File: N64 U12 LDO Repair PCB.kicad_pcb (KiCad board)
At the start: 2 copper layers, 8.5 x 7 mm, 5 parts, among them J1 Conn_01x05_Pin, U1 TLV78525PDBVR

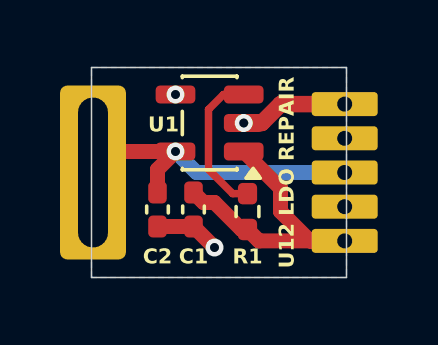
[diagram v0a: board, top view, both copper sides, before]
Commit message: Revision 1: Fix pin pitch
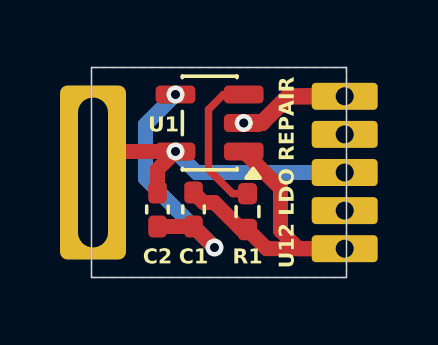
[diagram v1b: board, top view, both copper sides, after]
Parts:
- C2: value 4.7 uF -> 1 uF
- J1: footprint Custom:CustomAdapter_TO-252-5 -> Custom:CustomAdapter_SharpPQ7VZ5
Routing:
- net GND: track 5.82 -> 12.4 mm
- net +3V3: track 10.9 -> 11.4 mm
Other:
- board text added: "Rev. 1"
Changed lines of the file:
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@@
 			)
 		)
-		(property "Value" "4.7 uF"
+		(property "Value" "1 uF"
 			(at 0 1.16 90)
 			(layer "F.Fab")
@@
 		)
 	)
-	(footprint "Custom:CustomAdapter_TO-252-5"
+	(footprint "Custom:CustomAdapter_SharpPQ7VZ5"
 		(layer "F.Cu")
 		(at 50 50 180)
@@
 		(tags "DPAK TO-252 DPAK-5 TO-252-5")
 		(property "Reference" "J1"
-			(at 0 -4.5 0)
+			(at 0 -4.5 180)
 			(layer "F.SilkS")
 			(hide yes)
@@
 		)
 		(property "Value" "Conn_01x05_Pin"
-			(at 0 4.5 0)
+			(at 0 4.5 180)
 			(layer "F.Fab")
 			(effects
@@
 		)
 		(property "Datasheet" ""
-			(at 0 0 0)
+			(at 0 0 180)
 			(layer "F.Fab")
 			(hide yes)
@@
 		)
 		(property "Description" "Generic connector, single row, 01x05, script generated"
-			(at 0 0 0)
+			(at 0 0 180)
 			(layer "F.Fab")
 			(hide yes)
@@
 		)
 		(property "KiLib_Generator" "package/TO_SOT/SMD"
-			(at 0 0 0)
+			(at 0 0 180)
 			(layer "F.SilkS")
 			(hide yes)
@@
 		(sheetname "/")
 		(sheetfile "N64 U12 LDO Repair PCB.kicad_sch")
-		(attr smd exclude_from_bom allow_missing_courtyard dnp)
+		(attr smd allow_missing_courtyard dnp)
 		(duplicate_pad_numbers_are_jumpers no)
 		(fp_line
@@
 		)
 		(fp_text user "${REFERENCE}"
-			(at 0 0 0)
+			(at 0 0 180)
 			(layer "F.Fab")
 			(effects
@@
 		)
 		(pad "1" thru_hole roundrect
-			(at -5.04 -2.28 180)
-			(size 2.2 0.8)
-			(drill 0.5)
+			(at -5.04 -2.54 180)
+			(size 2.2 0.9)
+			(drill 0.6)
 			(property pad_prop_castellated)
 			(layers "*.Cu" "*.Mask")
@@
 		)
 		(pad "2" thru_hole roundrect
-			(at -5.04 -1.14 180)
-			(size 2.2 0.8)
-			(drill 0.5)
+			(at -5.04 -1.27 180)
+			(size 2.2 0.9)
+			(drill 0.6)
 			(property pad_prop_castellated)
 			(layers "*.Cu" "*.Mask")
@@
 		(pad "3" thru_hole roundrect
 			(at -5.04 0 180)
-			(size 2.2 0.8)
-			(drill 0.5)
+			(size 2.2 0.9)
+			(drill 0.6)
 			(property pad_prop_castellated)
 			(layers "*.Cu" "*.Mask")
@@
 		)
 		(pad "4" thru_hole roundrect
-			(at -5.04 1.14 180)
-			(size 2.2 0.8)
-			(drill 0.5)
+			(at -5.04 1.27 180)
+			(size 2.2 0.9)
+			(drill 0.6)
 			(property pad_prop_castellated)
 			(layers "*.Cu" "*.Mask")
@@
 		)
 		(pad "5" thru_hole roundrect
-			(at -5.04 2.28 180)
-			(size 2.2 0.8)
-			(drill 0.5)
+			(at -5.04 2.54 180)
+			(size 2.2 0.9)
+			(drill 0.6)
 			(property pad_prop_castellated)
 			(layers "*.Cu" "*.Mask")
@@
 		)
 	)
-	(segment
-		(start 51.735 51.835)
-		(end 51.8 51.9)
+	(gr_text "Rev. 1"
+		(at 51.1 53.2 -0)
+		(layer "B.SilkS")
+		(effects
+			(font
+				(size 0.5 0.5)
+				(thickness 0.1)
+				(bold yes)
+			)
+			(justify bottom mirror)
+		)
+	)
+	(segment
+		(start 48.835 50.7)
+		(end 48.8 50.665)
+		(width 0.5)
+		(layer "F.Cu")
+		(net "+2V5")
+	)
+	(segment
+		(start 47.35 49.3)
+		(end 46.65 50)
 		(width 0.2)
 		(layer "F.Cu")
-		(net "+3V3")
-	)
-	(segment
-		(start 52.9 51.3)
-		(end 52.9 50.525)
-		(width 0.5)
-		(layer "F.Cu")
-		(net "+3V3")
-	)
-	(segment
-		(start 55.04 52.28)
-		(end 52.18 52.28)
-		(width 0.5)
-		(layer "F.Cu")
-		(net "+3V3")
-	)
-	(segment
-		(start 51.6 51.9)
-		(end 50.7 51)
-		(width 0.5)
-		(layer "F.Cu")
-		(net "+3V3")
-	)
-	(segment
-		(start 55.04 52.28)
-		(end 53.88 52.28)
-		(width 0.5)
-		(layer "F.Cu")
-		(net "+3V3")
-	)
-	(segment
-		(start 53.88 52.28)
-		(end 52.9 51.3)
-		(width 0.5)
-		(layer "F.Cu")
-		(net "+3V3")
-	)
-	(segment
-		(start 50.7 51)
-		(end 50.335 51)
-		(width 0.5)
-		(layer "F.Cu")
-		(net "+3V3")
-	)
-	(segment
-		(start 52.18 52.28)
-		(end 51.8 51.9)
-		(width 0.5)
-		(layer "F.Cu")
-		(net "+3V3")
-	)
-	(segment
-		(start 51.8 51.9)
-		(end 51.6 51.9)
-		(width 0.5)
-		(layer "F.Cu")
-		(net "+3V3")
-	)
-	(segment
-		(start 50.335 51)
-		(end 50 50.665)
-		(width 0.5)
-		(layer "F.Cu")
-		(net "+3V3")
-	)
-	(segment
-		(start 52.9 50.525)
-		(end 51.675 49.3)
-		(width 0.5)
-		(layer "F.Cu")
-		(net "+3V3")
-	)
-	(segment
-		(start 55.04 47.72)
-		(end 52.90554 47.72)
+		(net "+2V5")
+	)
+	(segment
+		(start 49.4 49.3)
+		(end 47.35 49.3)
+		(width 0.5)
+		(layer "F.Cu")
+		(net "+2V5")
+	)
+	(segment
+		(start 48.8 49.9)
+		(end 49.4 49.3)
+		(width 0.5)
+		(layer "F.Cu")
+		(net "+2V5")
+	)
+	(segment
+		(start 48.8 50.665)
+		(end 48.8 49.9)
+		(width 0.5)
+		(layer "F.Cu")
+		(net "+2V5")
+	)
+	(via
+		(at 49.4 49.3)
+		(size 0.6)
+		(drill 0.3)
+		(layers "F.Cu" "B.Cu")
+		(net "+2V5")
+	)
+	(segment
+		(start 50.1 50)
+		(end 55 50)
+		(width 0.5)
+		(layer "B.Cu")
+		(net "+2V5")
+	)
+	(segment
+		(start 49.4 49.3)
+		(end 50.1 50)
+		(width 0.5)
+		(layer "B.Cu")
+		(net "+2V5")
+	)
+	(segment
+		(start 52.27554 48.35)
+		(end 51.675 48.35)
 		(width 0.55)
 		(layer "F.Cu")
@@
 	)
 	(segment
-		(start 52.90554 47.72)
-		(end 52.27554 48.35)
+		(start 55.04 47.46)
+		(end 53.16554 47.46)
 		(width 0.55)
 		(layer "F.Cu")
@@
 	)
 	(segment
-		(start 52.27554 48.35)
-		(end 51.675 48.35)
+		(start 53.16554 47.46)
+		(end 52.27554 48.35)
 		(width 0.55)
 		(layer "F.Cu")
@@
 	)
 	(segment
-		(start 48.835 50.7)
-		(end 48.8 50.665)
-		(width 0.5)
-		(layer "F.Cu")
-		(net "+2V5")
-	)
-	(segment
-		(start 47.35 49.3)
-		(end 46.65 50)
+		(start 48.4 50.2)
+		(end 50.7 52.5)
+		(width 0.5)
+		(layer "B.Cu")
+		(net "GND")
+	)
+	(segment
+		(start 48.4 48.4)
+		(end 48.4 50.2)
+		(width 0.5)
+		(layer "B.Cu")
+		(net "GND")
+	)
+	(segment
+		(start 49.4 47.4)
+		(end 48.4 48.4)
+		(width 0.5)
+		(layer "B.Cu")
+		(net "GND")
+	)
+	(segment
+		(start 51.735 51.835)
+		(end 51.8 51.9)
 		(width 0.2)
 		(layer "F.Cu")
-		(net "+2V5")
-	)
-	(segment
-		(start 49.4 49.3)
-		(end 47.35 49.3)
-		(width 0.5)
-		(layer "F.Cu")
-		(net "+2V5")
-	)
-	(segment
-		(start 48.8 49.9)
-		(end 49.4 49.3)
-		(width 0.5)
-		(layer "F.Cu")
-		(net "+2V5")
-	)
-	(segment
-		(start 48.8 50.665)
-		(end 48.8 49.9)
-		(width 0.5)
-		(layer "F.Cu")
-		(net "+2V5")
-	)
-	(via
-		(at 49.4 49.3)
-		(size 0.6)
-		(drill 0.3)
-		(layers "F.Cu" "B.Cu")
-		(net "+2V5")
-	)
-	(segment
-		(start 50.1 50)
-		(end 55 50)
-		(width 0.5)
-		(layer "B.Cu")
-		(net "+2V5")
-	)
-	(segment
-		(start 49.4 49.3)
-		(end 50.1 50)
-		(width 0.5)
-		(layer "B.Cu")
-		(net "+2V5")
-	)
-	(segment
+		(net "+3V3")
+	)
+	(segment
+		(start 55.04 52.54)
+		(end 52.44 52.54)
+		(width 0.5)
+		(layer "F.Cu")
+		(net "+3V3")
+	)
+	(segment
+		(start 51.6 51.9)
+		(end 50.7 51)
+		(width 0.5)
+		(layer "F.Cu")
+		(net "+3V3")
+	)
+	(segment
+		(start 52.9 51.94)
+		(end 53.5 52.54)
+		(width 0.5)
+		(layer "F.Cu")
+		(net "+3V3")
+	)
+	(segment
+		(start 50.7 51)
+		(end 50.335 51)
+		(width 0.5)
+		(layer "F.Cu")
+		(net "+3V3")
+	)
+	(segment
+		(start 51.8 51.9)
+		(end 51.6 51.9)
+		(width 0.5)
+		(layer "F.Cu")
+		(net "+3V3")
+	)
+	(segment
+		(start 50.335 51)
+		(end 50 50.665)
+		(width 0.5)
+		(layer "F.Cu")
+		(net "+3V3")
+	)
+	(segment
+		(start 51.675 49.3)
+		(end 52.9 50.525)
+		(width 0.5)
+		(layer "F.Cu")
+		(net "+3V3")
+	)
+	(segment
+		(start 52.44 52.54)
+		(end 51.8 51.9)
+		(width 0.5)
+		(layer "F.Cu")
+		(net "+3V3")
+	)
+	(segment
+		(start 53.5 52.54)
+		(end 55.04 52.54)
+		(width 0.5)
+		(layer "F.Cu")
+		(net "+3V3")
+	)
+	(segment
+		(start 52.9 50.525)
+		(end 52.9 51.94)
+		(width 0.5)
+		(layer "F.Cu")
+		(net "+3V3")
+	)
+	(segment
